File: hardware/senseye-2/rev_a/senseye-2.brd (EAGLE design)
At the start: 149.8 x 55.3 mm, 15 parts, among them U1 ADC121S101, U2 ADC121S101, U3 ADC121S101

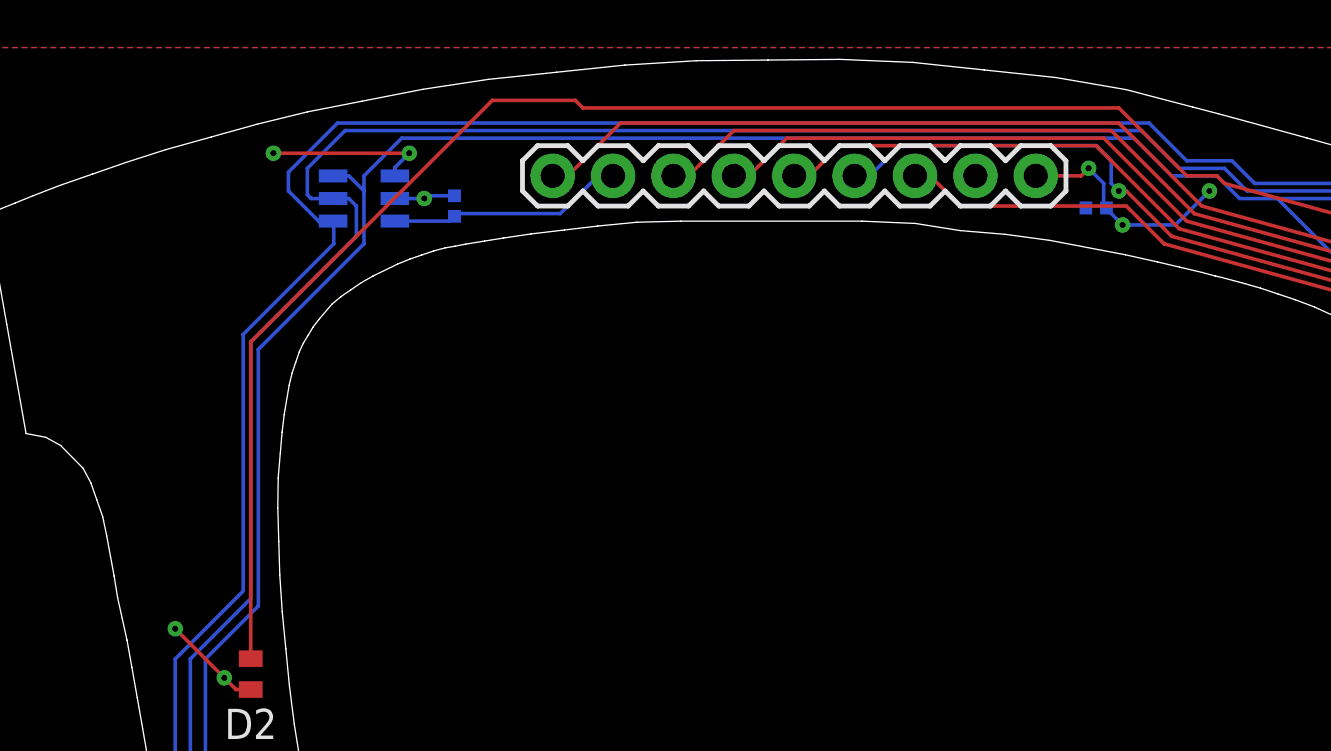
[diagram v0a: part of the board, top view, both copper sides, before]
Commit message: added power header
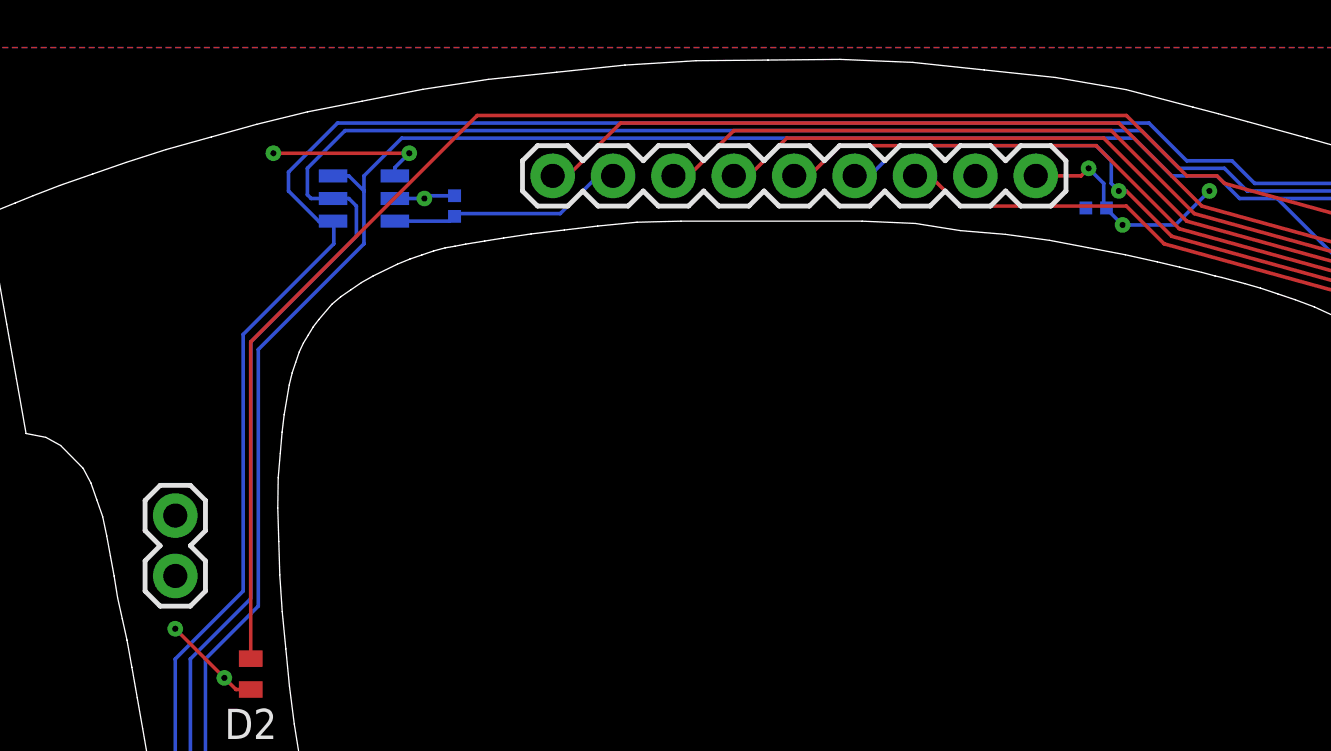
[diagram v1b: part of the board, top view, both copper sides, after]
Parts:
- added JP4: (no value), SparkFun-Connectors:1X02
- moved U1 57.8 mm to (60.3, -7.62)
- moved U2 57.8 mm to (21.3, -50.2)
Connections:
- net !CS0: now also U1.4; no longer U2.4
- net !CS1: now also U2.4; no longer U1.4
- net ANALOG0: now also U1.3; no longer U2.3
- net GND: now also JP4.2
- net N$1: now also U2.3; no longer U1.3
- net VCC: now also JP4.1
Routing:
- net LED: track 206.6 -> 206.1 mm
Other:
- board text added: "GND"
- board text added: "VCC"
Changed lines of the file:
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@@
 <setting verticaltext="up"/>
 </settings>
-<grid distance="0.0125" unitdist="inch" unit="inch" style="lines" multiple="1" display="yes" altdistance="0.003125" altunitdist="inch" altunit="inch"/>
+<grid distance="0.0125" unitdist="inch" unit="mm" style="lines" multiple="1" display="yes" altdistance="0.003125" altunitdist="inch" altunit="inch"/>
 <layers>
 <layer number="1" name="Top" color="4" fill="1" visible="yes" active="yes"/>
@@
 <wire x1="137.356921875" y1="-31.47831875" x2="137.07476875" y2="-32.908896875" width="0" layer="20"/>
 <wire x1="137.07476875" y1="-32.908896875" x2="136.762296875" y2="-34.149303125" width="0" layer="20"/>
+<text x="6.6675" y="-22.86" size="0.5" layer="26" font="vector" ratio="10" rot="MR90">VCC</text>
+<text x="6.6675" y="-20.32" size="0.5" layer="26" font="vector" ratio="10" rot="MR90">GND</text>
+<text x="45.72" y="-3.81" size="0.5" layer="26" ratio="10" rot="MR0">GND</text>
+<text x="86.36" y="-6.6675" size="0.5" layer="26" ratio="10" rot="MR0">GND</text>
+<text x="27.305" y="-53.6575" size="0.5" layer="26" ratio="10" rot="MR0">GND</text>
 </plain>
 <attributes>
@@
 </autorouter>
 <elements>
-<element name="U1" library="chips" package="SOT-23-6" value="ADC121S101" x="21.2725" y="-50.165" smashed="yes" rot="MR270">
+<element name="U2" library="chips" package="SOT-23-6" value="ADC121S101" x="21.2725" y="-50.165" smashed="yes" rot="MR270">
 <attribute name="MOUSER" value="926-AD121S101CISDNPB" x="26.3525" y="-74.295" size="1.778" layer="28" rot="MR270" display="off"/>
 <attribute name="NEWARK" value="96K6188" x="26.3525" y="-74.295" size="1.778" layer="28" rot="MR270" display="off"/>
@@
 <attribute name="NAME" x="21.59" y="-48.26" size="1.27" layer="26" font="vector" rot="MR0"/>
 </element>
-<element name="U2" library="chips" package="SOT-23-6" value="ADC121S101" x="60.325" y="-7.62" smashed="yes" rot="MR270">
+<element name="U1" library="chips" package="SOT-23-6" value="ADC121S101" x="60.325" y="-7.62" smashed="yes" rot="MR270">
 <attribute name="MOUSER" value="926-AD121S101CISDNPB" x="65.405" y="-44.45" size="1.778" layer="28" rot="MR270" display="off"/>
 <attribute name="NEWARK" value="96K6188" x="65.405" y="-44.45" size="1.778" layer="28" rot="MR270" display="off"/>
@@
 <attribute name="NAME" x="20.6375" y="-5.6515" size="1.27" layer="26" font="vector" ratio="10" rot="MR0" align="bottom-center"/>
 </element>
+<element name="JP4" library="SparkFun-Connectors" package="1X02" value="" x="8.89" y="-22.225" smashed="yes" rot="R90">
+<attribute name="VALUE" x="12.065" y="-23.495" size="1.27" layer="27" rot="R90"/>
+</element>
 </elements>
 <signals>
@@
 <contactref element="JP1" pad="9"/>
 <contactref element="JP3" pad="9"/>
+<contactref element="U1" pad="2"/>
+<contactref element="R1" pad="2"/>
 <contactref element="U2" pad="2"/>
-<contactref element="R1" pad="2"/>
-<contactref element="U1" pad="2"/>
 <contactref element="JP6" pad="GND1"/>
 <contactref element="JP6" pad="GND0"/>
@@
 <wire x1="62.23" y1="-7.9375" x2="61.9125" y2="-7.62" width="0.1524" layer="16"/>
 <wire x1="61.9125" y1="-7.62" x2="61.625" y2="-7.62" width="0.1524" layer="16"/>
+<contactref element="JP4" pad="2"/>
 </signal>
 <signal name="VCC">
 <contactref element="JP1" pad="8"/>
 <contactref element="JP3" pad="8"/>
-<contactref element="U2" pad="1"/>
+<contactref element="U1" pad="1"/>
 <contactref element="D2" pad="1"/>
 <contactref element="D1" pad="1"/>
-<contactref element="U1" pad="1"/>
+<contactref element="U2" pad="1"/>
 <contactref element="C1" pad="2"/>
 <contactref element="C3" pad="2"/>
@@
 <wire x1="140.335" y1="-20.32" x2="140.0175" y2="-20.6375" width="0.1524" layer="1"/>
 <via x="140.0175" y="-20.6375" extent="1-16" drill="0.254"/>
+<contactref element="JP4" pad="1"/>
 </signal>
 <signal name="RESP0">
@@
 <signal name="ANALOG0">
 <contactref element="JP1" pad="2"/>
-<contactref element="U2" pad="3"/>
+<contactref element="U1" pad="3"/>
 <contactref element="R1" pad="1"/>
 <wire x1="67.945" y1="-8.255" x2="67.31" y2="-8.255" width="0.1524" layer="16"/>
@@
 </signal>
 <signal name="!CS0">
-<contactref element="U2" pad="4"/>
+<contactref element="U1" pad="4"/>
 <contactref element="JP6" pad="15"/>
 <wire x1="59.025" y1="-8.57" x2="59.025" y2="-9.495" width="0.1524" layer="16"/>
@@
 </signal>
 <signal name="!CS1">
-<contactref element="U1" pad="4"/>
+<contactref element="U2" pad="4"/>
 <contactref element="U3" pad="4"/>
 <contactref element="JP6" pad="16"/>
@@
 </signal>
 <signal name="SCLK">
+<contactref element="U2" pad="6"/>
 <contactref element="U1" pad="6"/>
-<contactref element="U2" pad="6"/>
 <contactref element="U3" pad="6"/>
 <contactref element="JP6" pad="18"/>
@@
 </signal>
 <signal name="SDATA">
+<contactref element="U1" pad="5"/>
 <contactref element="U2" pad="5"/>
-<contactref element="U1" pad="5"/>
 <contactref element="U3" pad="5"/>
 <contactref element="JP6" pad="17"/>
@@
 </signal>
 <signal name="N$1">
-<contactref element="U1" pad="3"/>
+<contactref element="U2" pad="3"/>
 <contactref element="R2" pad="1"/>
 <contactref element="JP2" pad="2"/>
@@
 <contactref element="JP6" pad="19"/>
 <wire x1="12.065" y1="-25.7025" x2="12.065" y2="-12.3825" width="0.1524" layer="1"/>
-<wire x1="12.065" y1="-12.3825" x2="22.225" y2="-2.2225" width="0.1524" layer="1"/>
-<wire x1="22.225" y1="-2.2225" x2="25.7175" y2="-2.2225" width="0.1524" layer="1"/>
-<wire x1="25.7175" y1="-2.2225" x2="26.035" y2="-2.54" width="0.1524" layer="1"/>
-<wire x1="26.035" y1="-2.54" x2="48.5775" y2="-2.54" width="0.1524" layer="1"/>
-<wire x1="48.5775" y1="-2.54" x2="51.435" y2="-5.3975" width="0.1524" layer="1"/>
 <wire x1="62.23" y1="-26.655" x2="62.23" y2="-24.13" width="0.1524" layer="1"/>
 <wire x1="62.23" y1="-24.13" x2="64.135" y2="-22.225" width="0.1524" layer="1"/>
@@
 <wire x1="140.6525" y1="-26.3525" x2="140.6525" y2="-31.75" width="0.1524" layer="1"/>
 <wire x1="140.6525" y1="-31.75" x2="137.16" y2="-41.275" width="0.1524" layer="1"/>
+<wire x1="12.065" y1="-12.3825" x2="21.59" y2="-2.8575" width="0.1524" layer="1"/>
+<wire x1="21.59" y1="-2.8575" x2="48.895" y2="-2.8575" width="0.1524" layer="1"/>
+<wire x1="48.895" y1="-2.8575" x2="51.435" y2="-5.3975" width="0.1524" layer="1"/>
 </signal>
 </signals>

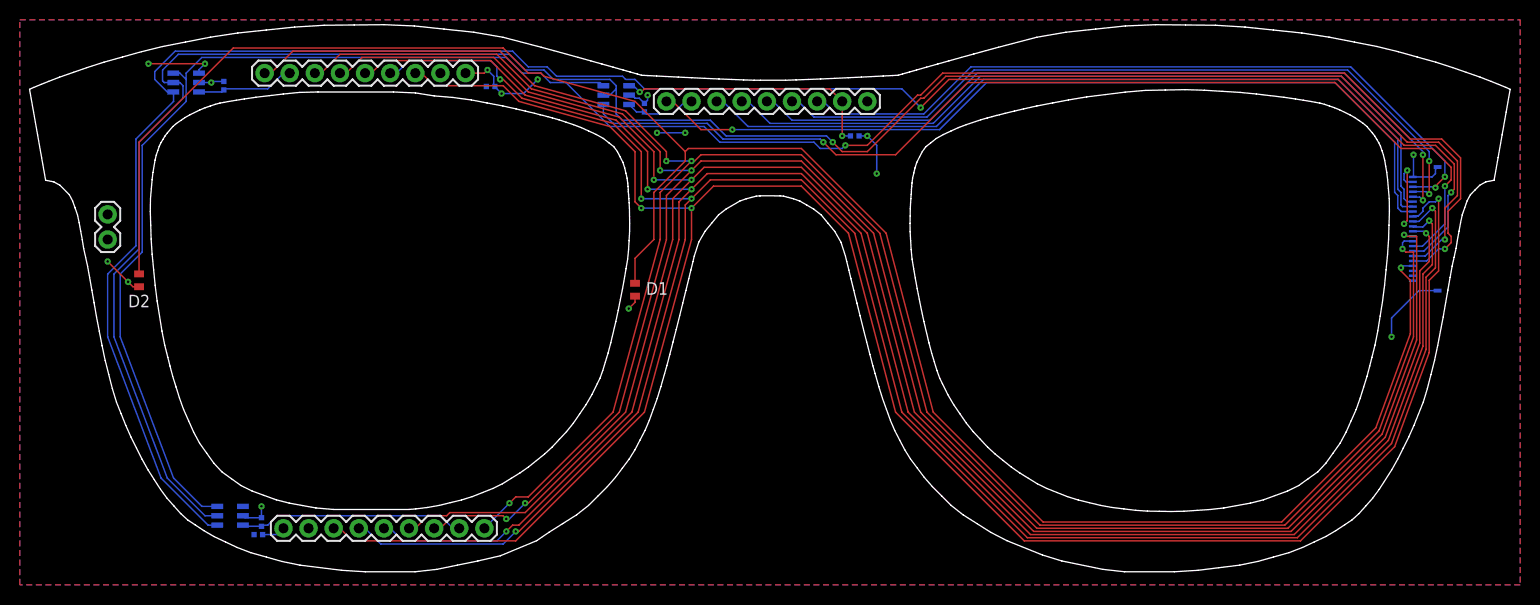
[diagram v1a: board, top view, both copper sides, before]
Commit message: using spi instead of i2c
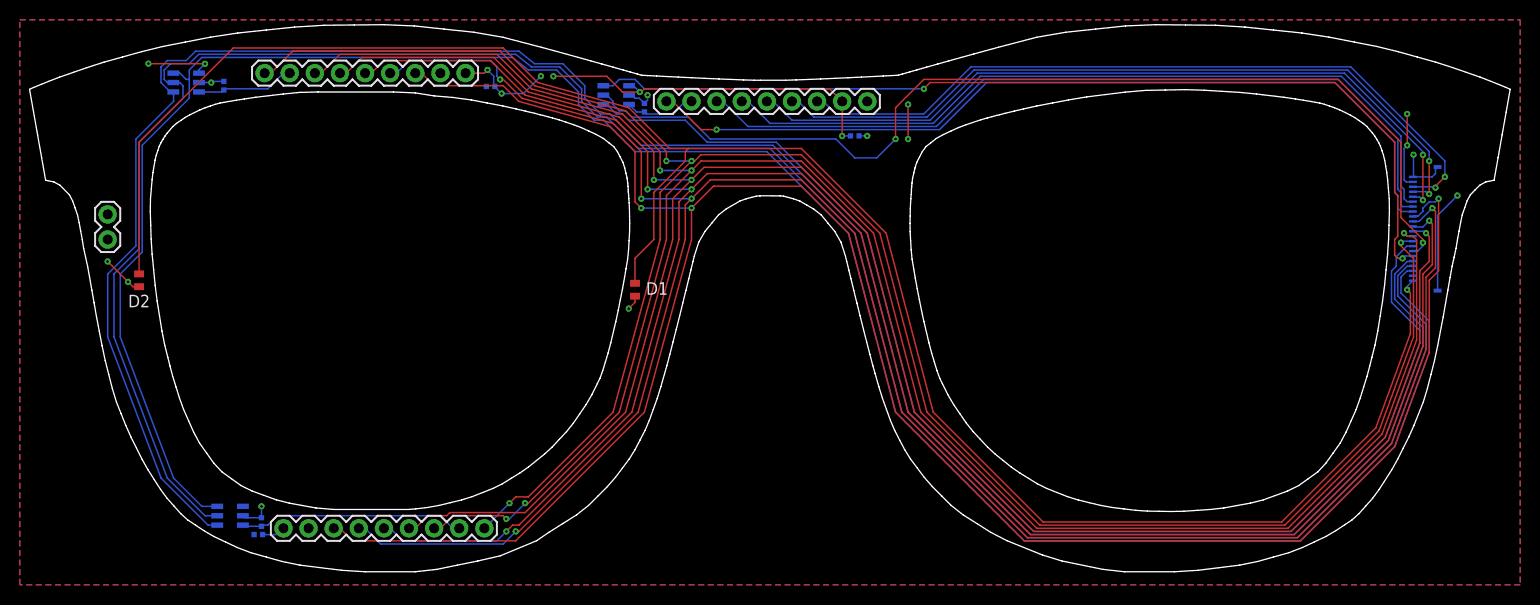
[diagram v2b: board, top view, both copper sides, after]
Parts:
- added U$1: (no value), logos:UMICH_SOLID_200MIL
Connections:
- removed net !CS1: JP6.16, U2.4, U3.4
- removed net SCLK: JP6.18, U1.6, U2.6, U3.6
- removed net SDATA: JP6.17, U1.5, U2.5, U3.5
- new net N$6: JP6.18, U2.4, U3.4
- new net SCLK0: JP6.17, U1.6
- new net SCLK1: JP6.20, U2.6, U3.6
- new net SDATA0: JP6.16, U1.5
- new net SDATA1: JP6.19, U2.5, U3.5
- net LED: now also JP6.22; no longer JP6.19
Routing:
- net N$6: track 0.00 -> 230.8 mm
- net SDATA1: track 0.00 -> 230.2 mm
- net SCLK1: track 0.00 -> 226.8 mm
- net SDATA: track 211.6 -> 0.00 mm, vias 2 -> 0
- net SCLK: track 209.7 -> 0.00 mm, vias 2 -> 0
- net !CS1: track 204.3 -> 0.00 mm, vias 2 -> 0
- net SDATA0: track 0.00 -> 103.9 mm, vias 0 -> 2
- net SCLK0: track 0.00 -> 97.2 mm, vias 0 -> 2
- net !CS0: track 105.1 -> 129.8 mm, vias 2 -> 0
- net VCC: track 47.1 -> 60.1 mm, vias 9 -> 12
- net GND: track 41.5 -> 37.7 mm, vias 12 -> 9
- net LED: track 206.1 -> 203.7 mm
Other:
- board text added: "2016/02/06"
- board text added: "N.Jackson"
- board text added: "RevA"
- board text added: "SensEye 2"

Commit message: added drills for hinges
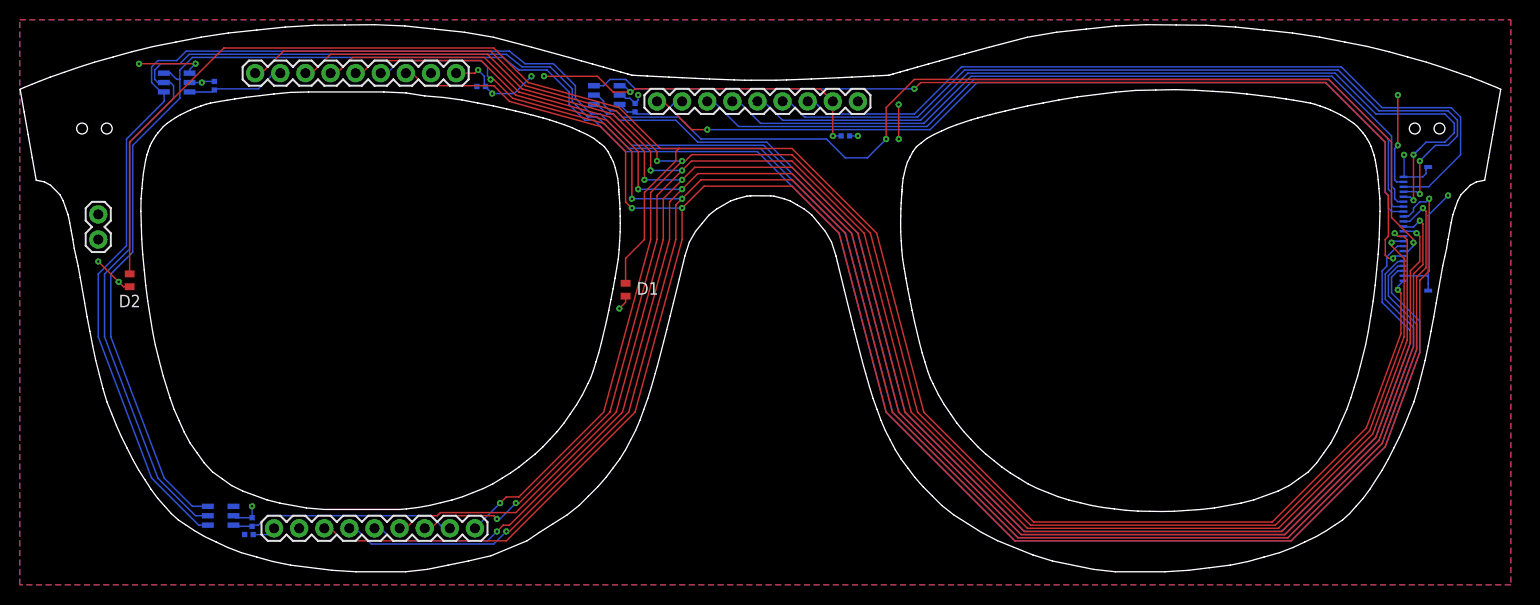
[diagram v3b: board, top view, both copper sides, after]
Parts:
- moved C1 0.95 mm to (83.5, -11.7)
- moved C3 0.95 mm to (23.2, -52.1)
- moved C5 0.95 mm to (46.7, -6.75)
- moved JP1 0.95 mm to (64.5, -8.26)
- moved JP2 0.95 mm to (46.0, -51.4)
- moved JP3 0.95 mm to (23.8, -5.40)
- moved JP4 0.95 mm to (7.94, -22.2)
- moved R1 0.95 mm to (62.2, -8.89)
- moved R2 0.95 mm to (23.5, -50.8)
- moved R3 0.95 mm to (19.7, -6.67)
- moved U$1 0.95 mm to (78.7, -14.9)
- moved U1 0.95 mm to (59.4, -7.62)
- moved U2 0.95 mm to (20.3, -50.2)
- moved U3 0.95 mm to (15.9, -6.35)
- moved D2 0.95 mm to (11.1, -26.4)
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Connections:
- net GND: now also JP6.21
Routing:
- net RESV0: track 78.5 -> 88.0 mm
- net INCP0: track 76.5 -> 84.5 mm
- net RESP0: track 75.4 -> 81.6 mm, vias 2 -> 0
- net GND: track 37.7 -> 40.2 mm
- net VCC: track 60.1 -> 62.0 mm
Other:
- outline, holes or cut-outs redrawn
